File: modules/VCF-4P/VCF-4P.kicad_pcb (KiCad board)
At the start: 2 copper layers, 111.5 x 108.2 mm, 36 parts, among them J1 WQP-PJ398, J10 Conn_Front_Left_Top, J11 Conn_Back_Right_Top, J12 Conn_Front_Right, J13 Conn_Back_Left, J2 WQP-PJ398, J3 WQP-PJ398, J4 WQP-PJ398, J5 WQP-PJ398, J6 WQP-PJ398, J7 WQP-PJ398, J8 WQP-PJ398, J9 Conn_Eurorack_16, U3 TL072

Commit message: VCF-4P: wip
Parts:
- removed C5: 10U, -lmp-misc:CP_Radial_D5.0mm_P2.50mm
- moved JP1 28.9 mm to (195.5, 123.2)
- moved H2 13.2 mm to (143.6, 38.9)
- moved H4 13.2 mm to (204.6, 38.9)
- moved H1 13.2 mm to (99.1, 38.9)
- moved H3 13.2 mm to (160.1, 38.9)
- moved C2 9.31 mm to (194.3, 128.3)
- moved C1 7.08 mm to (194.3, 138.9)
- moved G1 4.34 mm to (203.1, 45.1)
- moved G3 4.34 mm to (204.7, 49.8)
- moved J11 2.85 mm to (206.1, 56.9)
- moved J12 0.65 mm to (145.1, 95.2)
- moved J13 0.51 mm to (159.3, 95.2)
- moved J10 0.51 mm to (98.3, 59.7)
- moved RV1 0.30 mm to (107.7, 48.6)
- moved RV5 0.30 mm to (130.5, 48.6)
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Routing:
- net +5V: track 50.4 -> 0.00 mm
- net Net-(J9-Pad13): track 30.2 -> 8.94 mm
- net IN-GATE-BUS: track 10.4 -> 0.00 mm
- net -12V: track 20.8 -> 11.0 mm
- net +12V: track 16.5 -> 10.2 mm
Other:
- board size 111.5 x 108.2 mm -> 111.3 x 108.3 mm

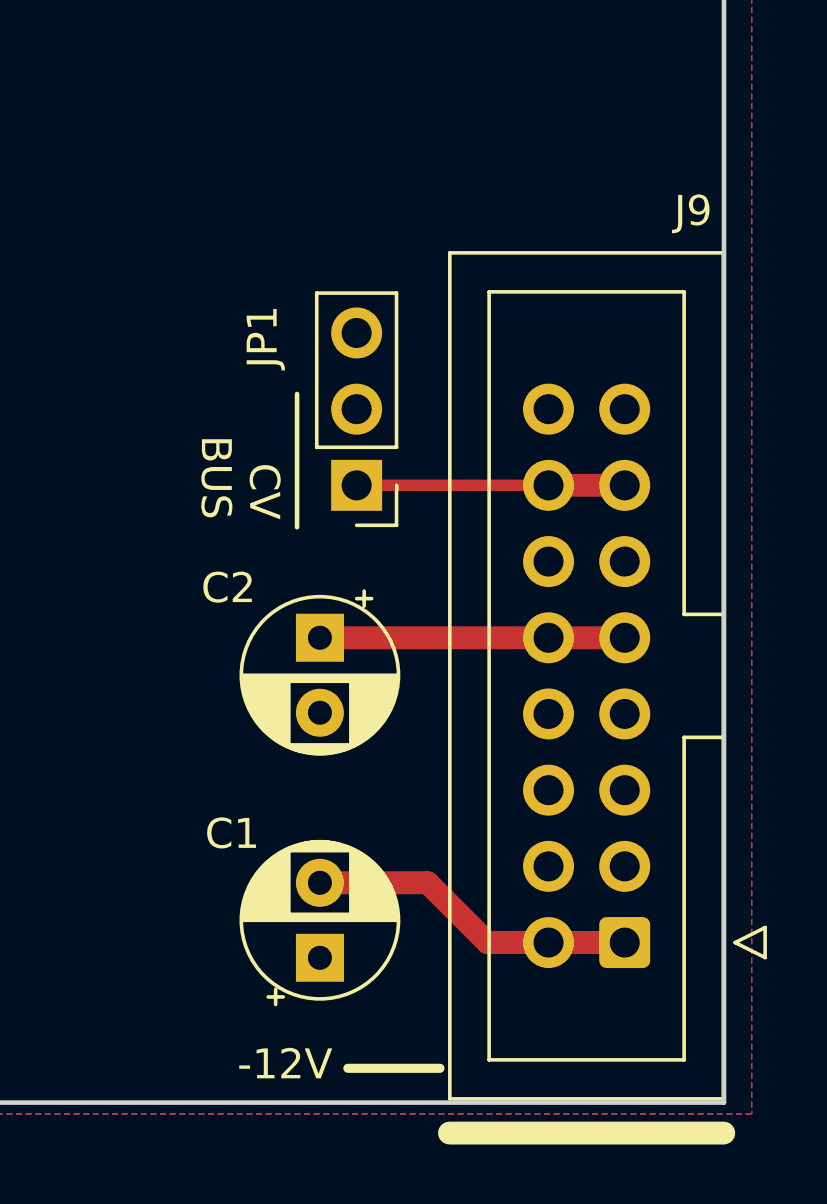
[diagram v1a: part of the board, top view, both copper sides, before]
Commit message: Add some KiCad temp files to .gitignore
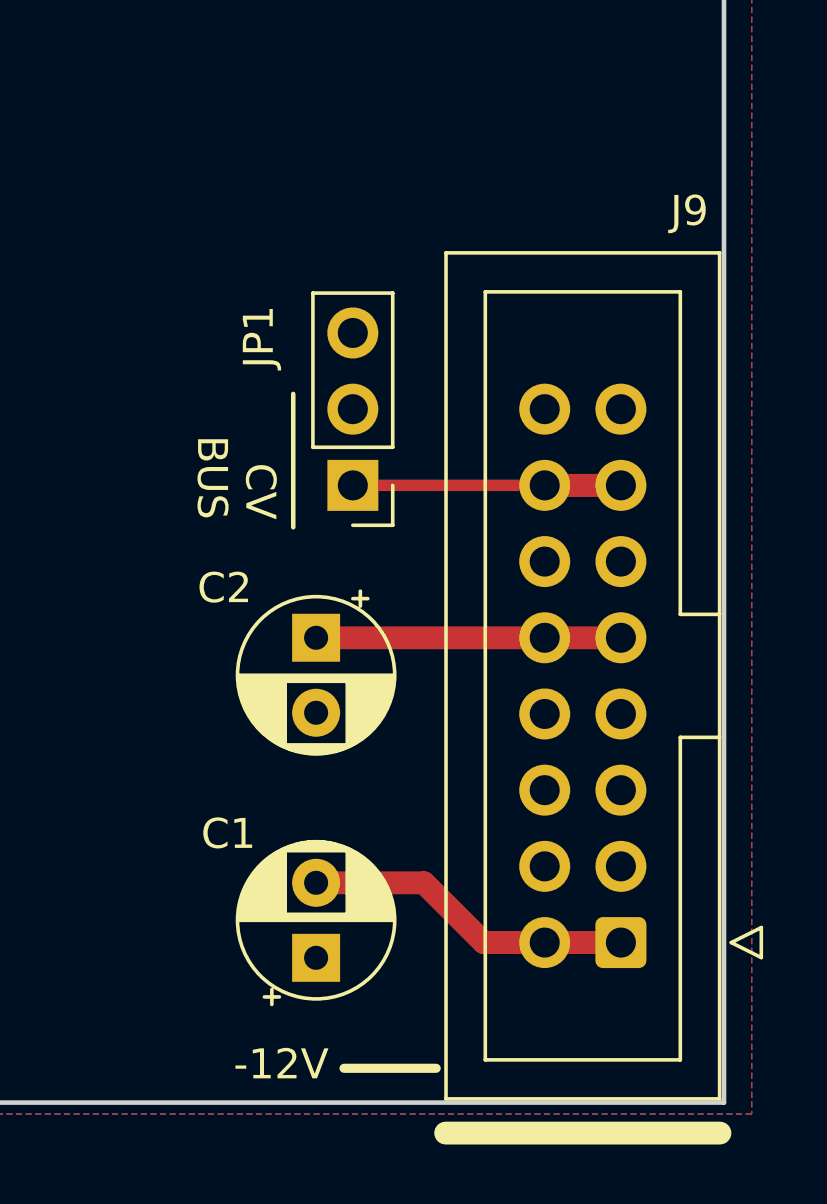
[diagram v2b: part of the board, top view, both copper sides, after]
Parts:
- moved C1 0.13 mm to (194.2, 138.9)
- moved C2 0.13 mm to (194.2, 128.3)
- moved J9 0.13 mm to (204.3, 138.4)
- moved JP1 0.13 mm to (195.4, 123.2)
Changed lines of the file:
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@@
   (net 46 "IN-CV-BUS")
   (footprint "-lmp-misc:CP_Radial_D5.0mm_P2.50mm" (layer "F.Cu")
-    (at 194.31 128.27 -90)
+    (at 194.183 128.27 -90)
     (descr "CP, Radial series, Radial, pin pitch=2.50mm, , diameter=5mm, Electrolytic Capacitor")
     (tags "CP Radial series Radial pin pitch 2.50mm  diameter 5mm Electrolytic Capacitor")
@@
     (property "Value2" "25 VDC")
     (attr through_hole)
-    (fp_text reference "C2" (at -1.651 3.048 180) (layer "F.SilkS")
+    (fp_text reference "C2" (at -1.651 3.048) (layer "F.SilkS")
       (effects (font (size 1 1) (thickness 0.15)))
     )
@@
   )
   (footprint "-lmp-misc:CP_Radial_D5.0mm_P2.50mm" (layer "F.Cu")
-    (at 194.31 138.938 90)
+    (at 194.183 138.938 90)
     (descr "CP, Radial series, Radial, pin pitch=2.50mm, , diameter=5mm, Electrolytic Capacitor")
     (tags "CP Radial series Radial pin pitch 2.50mm  diameter 5mm Electrolytic Capacitor")
@@
   )
   (footprint "-lmp-synth:IDC-Header-Eurorack-16-TH" (layer "F.Cu")
-    (at 204.47 138.43 180)
+    (at 204.343 138.43 180)
     (descr "Through-hole Eurorack 16-pin board power/CV/gate bus connector, shrouded")
     (tags "Through hole vertical IDC box header THT 2x08 2.54mm double row Eurorack")
@@
   )
   (footprint "-lmp-misc:PinHeader_1x03_P2.54mm_Vertical" (layer "F.Cu")
-    (at 195.534001 123.19 180)
+    (at 195.407001 123.19 180)
     (descr "Through hole straight pin header, 1x03, 2.54mm pitch, single row")
     (tags "Through hole pin header THT 1x03 2.54mm single row")
@@
     )
   )
-  (gr_line (start 193.548 124.587) (end 193.548 120.142) (layer "F.SilkS") (width 0.1524))
-  (gr_line (start 198.313396 142.621) (end 195.239996 142.621) (layer "F.SilkS") (width 0.3048))
+  (gr_line (start 193.421 124.587) (end 193.421 120.142) (layer "F.SilkS") (width 0.1524))
+  (gr_line (start 198.186396 142.621) (end 195.112996 142.621) (layer "F.SilkS") (width 0.3048))
   (gr_line (start 142.621 56.91) (end 149.733 56.91) (layer "Dwgs.User") (width 0.1016))
   (gr_line (start 206.06 53.707) (end 206.06 58.406) (layer "Dwgs.User") (width 0.1016))
@@
     (effects (font (size 1 1) (thickness 0.15)) (justify left))
   )
-  (gr_text "-12V" (at 194.731996 142.494) (layer "F.SilkS")
+  (gr_text "-12V" (at 194.604996 142.494) (layer "F.SilkS")
     (effects (font (size 1 1) (thickness 0.15)) (justify right))
   )
@@
     (effects (font (size 1.016 1.016) (thickness 0.1524)) (justify left))
   )
-  (gr_text "CV\nBUS" (at 191.643 124.333 270) (layer "F.SilkS")
+  (gr_text "CV\nBUS" (at 191.516 124.333 270) (layer "F.SilkS")
     (effects (font (size 1 1) (thickness 0.15)) (justify right))
   )
@@
     (effects (font (size 1 1) (thickness 0.15)) (justify left))
   )
-  (segment (start 204.47 128.27) (end 201.93 128.27) (width 0.762) (layer "F.Cu") (net 1))
-  (segment (start 201.93 128.27) (end 194.31 128.27) (width 0.762) (layer "F.Cu") (net 1))
-  (segment (start 197.906 136.438) (end 194.31 136.438) (width 0.762) (layer "F.Cu") (net 3))
-  (segment (start 199.898 138.43) (end 197.906 136.438) (width 0.762) (layer "F.Cu") (net 3))
-  (segment (start 201.93 138.43) (end 199.898 138.43) (width 0.762) (layer "F.Cu") (net 3))
-  (segment (start 204.47 138.43) (end 201.93 138.43) (width 0.762) (layer "F.Cu") (net 3))
-  (segment (start 201.93 123.19) (end 204.47 123.19) (width 0.762) (layer "F.Cu") (net 21))
-  (segment (start 195.534001 123.19) (end 201.93 123.19) (width 0.381) (layer "F.Cu") (net 21))
+  (segment (start 204.343 128.27) (end 201.803 128.27) (width 0.762) (layer "F.Cu") (net 1))
+  (segment (start 201.803 128.27) (end 194.183 128.27) (width 0.762) (layer "F.Cu") (net 1))
+  (segment (start 197.779 136.438) (end 194.183 136.438) (width 0.762) (layer "F.Cu") (net 3))
+  (segment (start 199.771 138.43) (end 197.779 136.438) (width 0.762) (layer "F.Cu") (net 3))
+  (segment (start 201.803 138.43) (end 199.771 138.43) (width 0.762) (layer "F.Cu") (net 3))
+  (segment (start 204.343 138.43) (end 201.803 138.43) (width 0.762) (layer "F.Cu") (net 3))
+  (segment (start 201.803 123.19) (end 204.343 123.19) (width 0.762) (layer "F.Cu") (net 21))
+  (segment (start 195.407001 123.19) (end 201.803 123.19) (width 0.381) (layer "F.Cu") (net 21))
   (zone (net 2) (net_name "GND") (layer "F.Cu") (hatch edge 0.508)
     (connect_pads (clearance 0.2032))

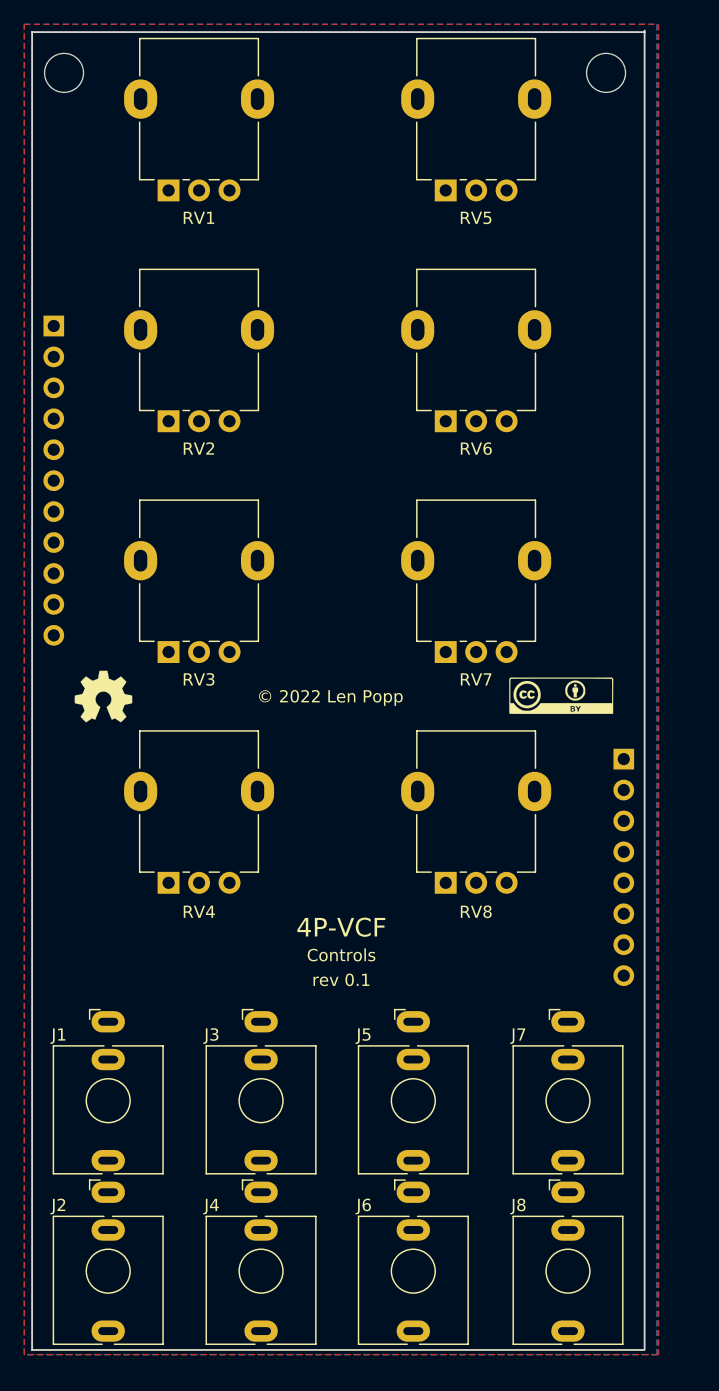
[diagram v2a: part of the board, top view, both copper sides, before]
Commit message: VCF-4P: fix some footprints & board outline
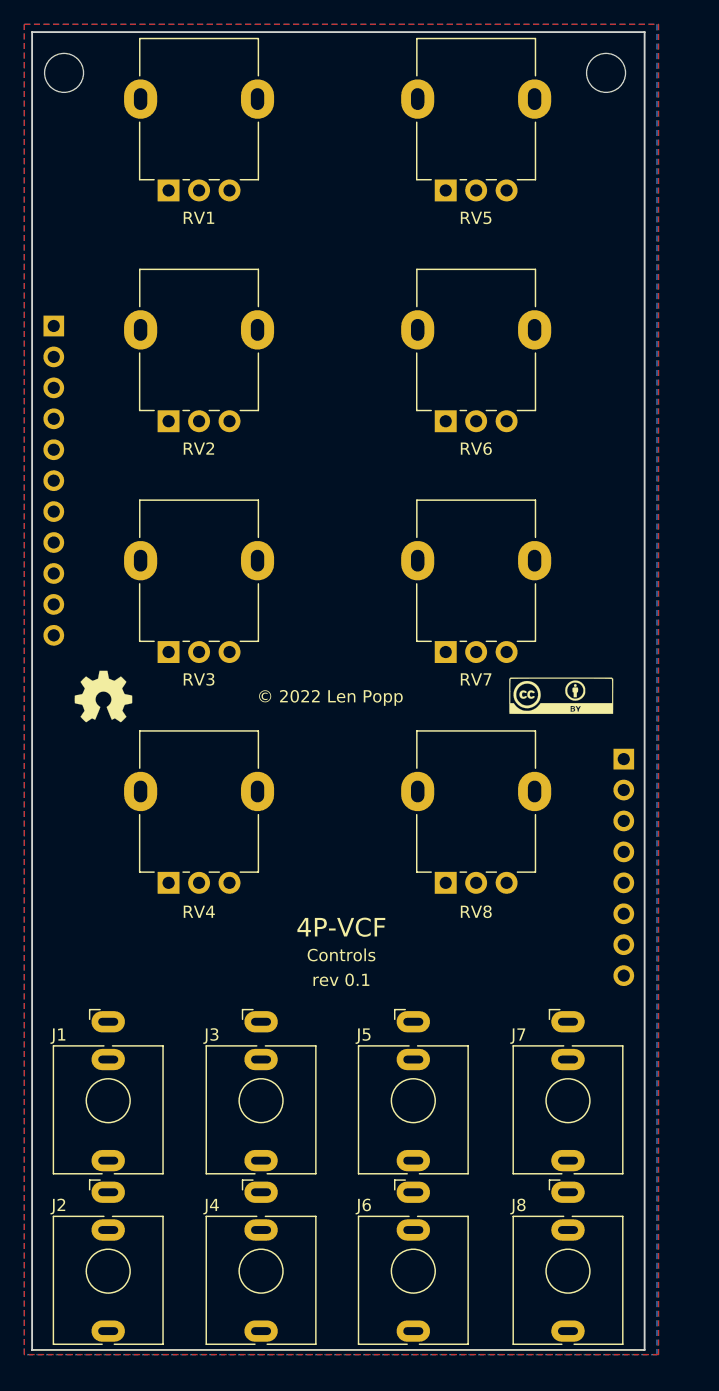
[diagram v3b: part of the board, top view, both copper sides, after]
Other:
- board size 111.3 x 108.3 mm -> 111.3 x 108.2 mm

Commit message: VCF-4P: PCB layout - wip
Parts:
- removed J2, J6: WQP-PJ398, -lmp-synth:Jack_3.5mm_QingPu_WQP-PJ398SM_Vertical
- removed the J8 at (140.5, 130.8)
- removed the RV2 at (107.7, 67.5)
- removed RV5: 100K, -lmp-synth:Potentiometer_Alpha_RD901F-40-00D_Single_Vertical
- removed the RV7 at (130.5, 86.5)
- removed U3: TL072, -lmp-misc:DIP-8_W7.62mm_LongPads
- added C10: 100N, -lmp-misc:C_Disc_D5.0mm_W2.5mm_P2.50mm, F.Cu at (261.4, 87.6)
- added C11: 100N, -lmp-misc:C_Disc_D5.0mm_W2.5mm_P2.50mm, F.Cu at (249.3, 80.2)
- added C5: 1N, -lmp-misc:C_Rect_Kemet_L7.2mm_W2.5mm_P5mm, F.Cu at (251.2, 96.5)
- added C6: 10U, -lmp-misc:C_Radial_D5.0mm_H5.0mm_P2.50mm, F.Cu at (262.2, 66.2)
- added C7: 1N, -lmp-misc:C_Rect_Kemet_L7.2mm_W2.5mm_P5mm, F.Cu at (240.8, 104.6)
- added C8: 1N, -lmp-misc:C_Rect_Kemet_L7.2mm_W2.5mm_P5mm, F.Cu at (249.9, 75.4)
- added C9: 1N, -lmp-misc:C_Rect_Kemet_L7.2mm_W2.5mm_P5mm, F.Cu at (252.1, 69.8)
- added R1: 1M, -lmp-misc:R_Axial_DIN0207_L6.3mm_D2.5mm_P7.62mm_Horizontal, F.Cu at (238.1, 78.6)
- added R10: 10K, -lmp-misc:R_Axial_DIN0207_L6.3mm_D2.5mm_P7.62mm_Horizontal, F.Cu at (250.2, 91.7)
- added R11: 10K, -lmp-misc:R_Axial_DIN0207_L6.3mm_D2.5mm_P7.62mm_Horizontal, F.Cu at (245.4, 52.8)
- added R12: 200R, -lmp-misc:R_Axial_DIN0207_L6.3mm_D2.5mm_P7.62mm_Horizontal, F.Cu at (245.4, 40.7)
- added R13: 10K, -lmp-misc:R_Axial_DIN0207_L6.3mm_D2.5mm_P7.62mm_Horizontal, F.Cu at (245.7, 56.9)
- added R14: 10K, -lmp-misc:R_Axial_DIN0207_L6.3mm_D2.5mm_P7.62mm_Horizontal, F.Cu at (239.4, 99.8)
- added R15: 200R, -lmp-misc:R_Axial_DIN0207_L6.3mm_D2.5mm_P7.62mm_Horizontal, F.Cu at (239.4, 95.7)
- added R16: 10K, -lmp-misc:R_Axial_DIN0207_L6.3mm_D2.5mm_P7.62mm_Horizontal, F.Cu at (226.9, 80.8)
- added R17: 100K, -lmp-misc:R_Axial_DIN0207_L6.3mm_D2.5mm_P7.62mm_Horizontal, F.Cu at (256.4, 60.9)
- added R18: 100K, -lmp-misc:R_Axial_DIN0207_L6.3mm_D2.5mm_P7.62mm_Horizontal, F.Cu at (227.3, 72.7)
- added R19: 120K, -lmp-misc:R_Axial_DIN0207_L6.3mm_D2.5mm_P7.62mm_Horizontal, F.Cu at (256.1, 52.8)
- added R2: 24K (15K?), -lmp-misc:R_Axial_DIN0207_L6.3mm_D2.5mm_P7.62mm_Horizontal, F.Cu at (239.4, 91.7)
- added R20: 100K, -lmp-misc:R_Axial_DIN0207_L6.3mm_D2.5mm_P7.62mm_Horizontal, F.Cu at (245.4, 48.8)
- added R21: 100K, -lmp-misc:R_Axial_DIN0207_L6.3mm_D2.5mm_P7.62mm_Horizontal, F.Cu at (216.1, 79.1)
- added R22: 158K, -lmp-misc:R_Axial_DIN0207_L6.3mm_D2.5mm_P7.62mm_Horizontal, F.Cu at (227.3, 76.8)
- added R23: 100K, -lmp-misc:R_Axial_DIN0207_L6.3mm_D2.5mm_P7.62mm_Horizontal, F.Cu at (251.0, 65.0)
- added R24: 100K, -lmp-misc:R_Axial_DIN0207_L6.3mm_D2.5mm_P7.62mm_Horizontal, F.Cu at (240.2, 70.5)
- added R25: 53K, -lmp-misc:R_Axial_DIN0207_L6.3mm_D2.5mm_P7.62mm_Horizontal, F.Cu at (250.2, 87.6)
- added R26: 20K, -lmp-misc:R_Axial_DIN0207_L6.3mm_D2.5mm_P7.62mm_Horizontal, F.Cu at (256.1, 44.7)
- added R27: 120K, -lmp-misc:R_Axial_DIN0207_L6.3mm_D2.5mm_P7.62mm_Horizontal, F.Cu at (256.4, 56.9)
- added R28: 30K, -lmp-misc:R_Axial_DIN0207_L6.3mm_D2.5mm_P7.62mm_Horizontal, F.Cu at (240.2, 66.5)
- added R29: 1K, -lmp-misc:R_Axial_DIN0207_L6.3mm_D2.5mm_P10.16mm_Horizontal, F.Cu at (216.1, 68.7)
- added R3: 16K, -lmp-misc:R_Axial_DIN0207_L6.3mm_D2.5mm_P7.62mm_Horizontal, F.Cu at (245.4, 44.7)
- added R4: 1K, -lmp-misc:R_Axial_DIN0207_L6.3mm_D2.5mm_P7.62mm_Horizontal, F.Cu at (256.1, 48.8)
- added R5: 10K, -lmp-misc:R_Axial_DIN0207_L6.3mm_D2.5mm_P7.62mm_Horizontal, F.Cu at (238.1, 74.6)
- added R6: 200R, -lmp-misc:R_Axial_DIN0207_L6.3mm_D2.5mm_P7.62mm_Horizontal, F.Cu at (239.4, 87.6)
- added R7: 10K, -lmp-misc:R_Axial_DIN0207_L6.3mm_D2.5mm_P7.62mm_Horizontal, F.Cu at (256.1, 40.7)
- added R8: 10K, -lmp-misc:R_Axial_DIN0207_L6.3mm_D2.5mm_P7.62mm_Horizontal, F.Cu at (229.4, 68.7)
- added R9: 200R, -lmp-misc:R_Axial_DIN0207_L6.3mm_D2.5mm_P7.62mm_Horizontal, F.Cu at (245.7, 60.9)
- added RV10: 5K, -lmp-synth:Potentiometer_Bourns_3296Y_Vertical, F.Cu at (241.1, 60.0)
- added RV9: 5K, -lmp-synth:Potentiometer_Bourns_3296Y_Vertical, F.Cu at (222.7, 72.6)
- added U1: SSI2140, -lmp-breakout:Breakout_DIP-20_W15.24mm, F.Cu at (216.1, 41.2)
- added U2: TL074, Package_DIP:DIP-14_W7.62mm, F.Cu at (234.6, 40.7)
- C1, C2: footprint -lmp-misc:CP_Radial_D5.0mm_P2.50mm -> -lmp-misc:CP_Radial_D4.0mm_P1.50mm
- H6: renamed from H4; value MountingHole_M3 -> Hole_M3
- J10: value Conn_Front_Left_Top -> Conn_Front_Left; footprint Connector_PinSocket_2.54mm:PinSocket_1x11_P2.54mm_Vertical -> -lmp-synth:PinSocket_Delptronics_Front; moved to F.Cu
- J11: value Conn_Back_Right_Top -> Conn_Back_Right; footprint Connector_PinSocket_2.54mm:PinSocket_1x11_P2.54mm_Vertical -> -lmp-synth:PinHeader_Delptronics_Back_8HP; moved to F.Cu
- J12: footprint Connector_PinSocket_2.54mm:PinSocket_1x08_P2.54mm_Vertical -> -lmp-synth:PinSocket_Delptronics_Front; moved to F.Cu
- J13: footprint Connector_PinSocket_2.54mm:PinSocket_1x08_P2.54mm_Vertical -> -lmp-synth:PinHeader_Delptronics_Back_8HP; moved to F.Cu
- RV2: renamed from RV4; footprint -lmp-synth:Potentiometer_Alpha_RD901F-40-00D_Single_Vertical -> -lmp-synth:Potentiometer_SongHuei_Single_Vertical
- RV8: footprint -lmp-synth:Potentiometer_Alpha_RD901F-40-00D_Single_Vertical -> -lmp-synth:Potentiometer_SongHuei_Single_Vertical
- moved C3 60.8 mm to (228.6, 88.7)
- moved C4 60.8 mm to (228.6, 92.7)
- moved J12 38.3 mm to (145.1, 56.9), turned to 0 degrees
- moved J13 38.3 mm to (159.3, 56.9), turned to 0 degrees
- moved C2 12.1 mm to (205.2, 133.3)
- moved C1 11.4 mm to (205.2, 141.6)
- moved JP1 10.9 mm to (206.1, 125.5)
- moved J9 5.65 mm to (198.7, 138.4)
- moved J10 2.78 mm to (98.3, 56.9), turned to 0 degrees
- turned J11 to 0 degrees
- renumbered J4 to J3, J3 to J5, J5 to J7, J7 to J8, RV3 to RV4, RV6 to RV7
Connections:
- J1 pad T: IN-GATE-1 -> IN-AUDIO
- J1 pad TN: IN-GATE-BUS -> IN-AUDIO-N
- J10 pad 1: IN-GATE-1 -> CV-FREQ-POT-LO
- J10 pad 10: +5V -> unconnected-(J10-Pad10)
- J10 pad 11: IN-GATE-BUS -> IN-AUDIO-POT-LO
- J10 pad 2: Net-(J10-Pad2) -> CV-FREQ-POT
- J10 pad 3: Net-(J10-Pad3) -> CV-FREQ-POT-HI
- J10 pad 4: Net-(J10-Pad4) -> IN-AUDIO
- J10 pad 5: Net-(J10-Pad5) -> IN-AUDIO-N
- J10 pad 6: Net-(J10-Pad6) -> unconnected-(J10-Pad6)
- J10 pad 7: Net-(J10-Pad7) -> unconnected-(J10-Pad7)
- J10 pad 8: Net-(J10-Pad8) -> unconnected-(J10-Pad8)
- J10 pad 9: Net-(J10-Pad9) -> unconnected-(J10-Pad9)
- J11 pad 1: IN-GATE-1 -> GND
- J11 pad 10: +5V -> unconnected-(J11-Pad10)
- J11 pad 11: IN-GATE-BUS -> GND
- J11 pad 2: Net-(J10-Pad2) -> CV-FREQ-POT
- J11 pad 3: Net-(J10-Pad3) -> +12V
- J11 pad 4: Net-(J10-Pad4) -> IN-AUDIO
- J11 pad 5: Net-(J10-Pad5) -> GND
- J11 pad 6: Net-(J10-Pad6) -> unconnected-(J11-Pad6)
- J11 pad 7: Net-(J10-Pad7) -> unconnected-(J11-Pad7)
- J11 pad 8: Net-(J10-Pad8) -> unconnected-(J11-Pad8)
- J11 pad 9: Net-(J10-Pad9) -> unconnected-(J11-Pad9)
- J12 pad 1: Net-(J12-Pad1) -> unconnected-(J12-Pad1)
- J12 pad 2: Net-(J12-Pad2) -> unconnected-(J12-Pad2)
- J12 pad 3: Net-(J12-Pad3) -> unconnected-(J12-Pad3)
- J12 pad 4: Net-(J12-Pad4) -> CV-RES-MOD-N
- J12 pad 5: Net-(J12-Pad5) -> CV-RES-MOD
- J12 pad 6: Net-(J12-Pad6) -> CV-RES-POT-HI
- J12 pad 7: Net-(J12-Pad7) -> CV-RES-POT
- J12 pad 8: GND -> CV-RES-POT-LO
- J13 pad 1: Net-(J12-Pad1) -> unconnected-(J13-Pad1)
- J13 pad 2: Net-(J12-Pad2) -> unconnected-(J13-Pad2)
- J13 pad 3: Net-(J12-Pad3) -> unconnected-(J13-Pad3)
- J13 pad 4: Net-(J12-Pad4) -> GND
- J13 pad 5: Net-(J12-Pad5) -> CV-RES-MOD
- J13 pad 6: Net-(J12-Pad6) -> +12V
- J13 pad 7: Net-(J12-Pad7) -> CV-RES-POT
- J3 pad T: unconnected-(J4-PadT) -> CV-FREQ-1VOCT
- J3 pad TN: unconnected-(J4-PadTN) -> CV-FREQ-1VOCT-N
- J5 pad T: unconnected-(J3-PadT) -> CV-FREQ-MOD
- J5 pad TN: unconnected-(J3-PadTN) -> CV-FREQ-MOD-N
- J7 pad T: IN-GATE-2 -> CV-RES-MOD
- J7 pad TN: IN-GATE-1 -> CV-RES-MOD-N
- J8 pad T: unconnected-(J7-PadT) -> OUT-AUDIO
- J9 pad 11: +5V -> unconnected-(J9-Pad11)
- J9 pad 12: +5V -> unconnected-(J9-Pad12)
- JP1 pad 2: IN-CV-BUS -> CV-BUS
- RV1 pad 1: GND -> CV-FREQ-POT-LO
- RV1 pad 2: IN-POT-A-1 -> CV-FREQ-POT
- RV1 pad 3: +5V -> CV-FREQ-POT-HI
- RV2 pad 1: GND -> CV-FREQ-MOD-POT-LO
- RV2 pad 2: IN-POT-R-1 -> CV-FREQ-MOD-ATTEN
- RV2 pad 3: +5V -> CV-FREQ-MOD-POT-HI
- RV4 pad 1: GND -> IN-AUDIO-POT-LO
- RV4 pad 2: IN-POT-S-1 -> IN-AUDIO-ATTEN
- RV4 pad 3: +5V -> IN-AUDIO-POT-HI
- RV7 pad 1: GND -> CV-RES-POT-LO
- RV7 pad 2: IN-POT-D-2 -> CV-RES-POT
- RV7 pad 3: +5V -> CV-RES-POT-HI
- RV8 pad 1: GND -> CV-RES-MOD-POT-LO
- RV8 pad 2: IN-POT-R-2 -> CV-RES-MOD-ATTEN
- RV8 pad 3: +5V -> CV-RES-MOD-POT-HI
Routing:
- net CV-BUS: track 0.00 -> 20.0 mm
- net +12V: track 10.2 -> 15.4 mm
- net -12V: track 11.0 -> 14.6 mm
- net Net-(J9-Pad13): track 8.94 -> 10.9 mm
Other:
- board text added: "TODO: Position the controls!"
- board text added: "TODO: Verify headers match control PCB"

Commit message: VCF-4P: PCB layout - wip
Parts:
- moved RV1 11.4 mm to (119.1, 48.6)
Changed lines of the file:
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@@
   )
   (footprint "-lmp-synth:Potentiometer_Alpha_RD901F-40-00D_Single_Vertical" (layer "F.Cu")
-    (at 107.73 48.56 90)
+    (at 119.126 48.56 90)
     (descr "Potentiometer, vertical, 9mm, single, http://www.taiwanalpha.com.tw/downloads?target=products&id=113")
     (tags "potentiometer vertical 9mm single")

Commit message: VCF-4P: PCB layout - wip
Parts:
- moved R19 111.2 mm to (170.8, 124.1), turned to 90 degrees
- moved R26 104.9 mm to (168.9, 103.0), turned to 90 degrees
- moved R20 101.5 mm to (177.4, 124.1), turned to 90 degrees
- moved G1 97.0 mm to (178.9, 139.1)
- moved R24 93.1 mm to (164.1, 124.1), turned to 90 degrees
- moved R27 92.8 mm to (185.3, 116.5), turned to -90 degrees
- moved R4 92.4 mm to (170.2, 82.5), turned to -90 degrees
- moved G3 88.8 mm to (178.9, 134.7)
- moved R17 88.0 mm to (175.5, 95.5), turned to -90 degrees
- moved R25 85.5 mm to (164.7, 90.2), turned to 90 degrees
- moved R3 84.5 mm to (174.1, 90.2), turned to 90 degrees
- moved R23 84.4 mm to (172.2, 95.4), turned to -90 degrees
- moved C11 83.6 mm to (165.9, 75.3), turned to 90 degrees
- moved U2 80.1 mm to (188.2, 106.1), turned to -90 degrees
- moved R28 77.4 mm to (188.6, 124.1), turned to 90 degrees
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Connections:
- JP1 pad 1: Net-(J9-Pad13) -> GND
- JP1 pad 3: GND -> Net-(J9-Pad13)
- U1 pad 17: Net-(R13-Pad2) -> Net-(R7-Pad2)
- U1 pad 18: Net-(C8-Pad1) -> Net-(C5-Pad1)
- U1 pad 19: Net-(R11-Pad2) -> Net-(R5-Pad2)
- U1 pad 4: Net-(R7-Pad2) -> Net-(R13-Pad2)
- U1 pad 5: Net-(C5-Pad1) -> Net-(C8-Pad1)
- U1 pad 6: Net-(R5-Pad2) -> Net-(R11-Pad2)
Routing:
- net +12V: track 15.4 -> 137.6 mm, vias 0 -> 2
- net CV-FREQ-POT: track 0.00 -> 87.4 mm, vias 0 -> 1
- net -12V: track 14.6 -> 96.6 mm
- net Net-(R16-Pad2): track 0.00 -> 52.6 mm, vias 0 -> 1
- net CV-FREQ-MOD-ATTEN: track 0.00 -> 50.8 mm, vias 0 -> 2
- net CV-FREQ-1VOCT: track 0.00 -> 44.7 mm, vias 0 -> 1
- net Net-(R5-Pad2): track 0.00 -> 42.0 mm
- net OUT-AUDIO: track 0.00 -> 39.3 mm
- net Net-(R14-Pad2): track 0.00 -> 37.5 mm
- net Net-(R25-Pad2): track 0.00 -> 34.9 mm
- net Net-(R24-Pad2): track 0.00 -> 34.4 mm
- net CV-RES-POT: track 0.00 -> 34.2 mm, vias 0 -> 1
- net IN-AUDIO-ATTEN: track 0.00 -> 33.5 mm, vias 0 -> 1
- net CV-RES-MOD: track 0.00 -> 29.6 mm
- net Net-(R13-Pad2): track 0.00 -> 26.0 mm
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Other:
- board text added: "TODO: Adjust control & connector positions"
- board text added: "TODO: Move refdes"
- board text added: "https://len42.github.io/Synth/"
- board text removed: "TODO: Position the controls!"
- board text removed: "https://len42.github.io/"
